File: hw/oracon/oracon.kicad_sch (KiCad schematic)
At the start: 108 parts, among them J2 SIM_Card, J3 USB_A, J4 Conn_Coaxial, J5 USB_C_Receptacle_USB2.0_16P, Q1 SS8050, Q2 SS8050, Q3 SS8050, Q5 SS8050, SW1 SW_Push, U1 TP5100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

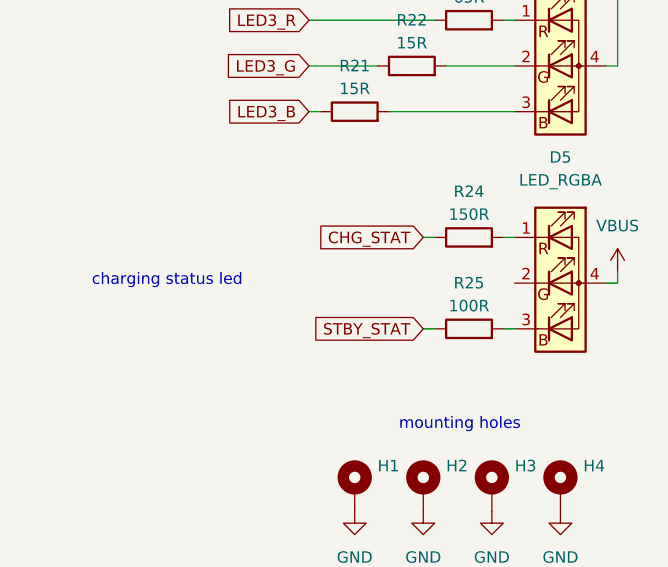
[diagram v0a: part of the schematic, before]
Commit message: Moved charging LED to green channel
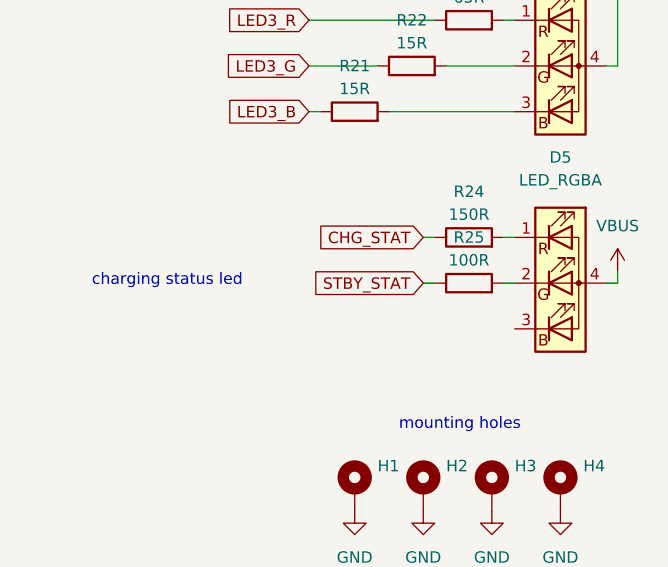
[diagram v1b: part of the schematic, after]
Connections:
- net at D5.2 (GK): now also R25.2
- net at D5.3 (BK): no longer R25.2
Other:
- moved on the sheet: R25
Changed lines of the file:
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@@
 	(wire
 		(pts
-			(xy 384.81 116.84) (xy 386.08 116.84)
-		)
-		(stroke
-			(width 0)
-			(type default)
-		)
-	)
-	(wire
-		(pts
 			(xy 278.13 270.51) (xy 278.13 271.78)
 		)
@@
 	(wire
 		(pts
+			(xy 384.81 111.76) (xy 386.08 111.76)
+		)
+		(stroke
+			(width 0)
+			(type default)
+		)
+	)
+	(wire
+		(pts
 			(xy 60.96 31.75) (xy 62.23 31.75)
 		)
@@
 	(wire
 		(pts
-			(xy 375.92 116.84) (xy 377.19 116.84)
-		)
-		(stroke
-			(width 0)
-			(type default)
-		)
-	)
-	(wire
-		(pts
 			(xy 209.55 36.83) (xy 209.55 19.05)
 		)
@@
 	(wire
 		(pts
+			(xy 375.92 111.76) (xy 377.19 111.76)
+		)
+		(stroke
+			(width 0)
+			(type default)
+		)
+	)
+	(wire
+		(pts
 			(xy 107.95 50.8) (xy 107.95 49.53)
 		)
@@
 		)
 	)
-	(global_label "STBY_STAT"
-		(shape input)
-		(at 375.92 116.84 180)
-		(fields_autoplaced yes)
-		(effects
-			(font
-				(size 1.27 1.27)
-			)
-			(justify right)
-		)
-		(property "Intersheetrefs" "${INTERSHEET_REFS}"
-			(at 363.1982 116.84 0)
-			(effects
-				(font
-					(size 1.27 1.27)
-				)
-				(justify right)
-				(hide yes)
-			)
-		)
-	)
 	(global_label "LED2_B"
 		(shape input)
@@
 		)
 	)
+	(global_label "STBY_STAT"
+		(shape input)
+		(at 375.92 111.76 180)
+		(fields_autoplaced yes)
+		(effects
+			(font
+				(size 1.27 1.27)
+			)
+			(justify right)
+		)
+		(property "Intersheetrefs" "${INTERSHEET_REFS}"
+			(at 363.1982 111.76 0)
+			(effects
+				(font
+					(size 1.27 1.27)
+				)
+				(justify right)
+				(hide yes)
+			)
+		)
+	)
 	(global_label "USB_SI_N"
 		(shape input)
@@
 	(symbol
 		(lib_id "Device:R")
-		(at 381 116.84 90)
+		(at 381 111.76 90)
 		(unit 1)
 		(exclude_from_sim no)
@@
 		(fields_autoplaced yes)
 		(property "Reference" "R25"
-			(at 381 111.76 90)
+			(at 381 106.68 90)
 			(effects
 				(font
@@
 		)
 		(property "Value" "100R"
-			(at 381 114.3 90)
+			(at 381 109.22 90)
 			(effects
 				(font
@@
 		)
 		(property "Footprint" "Resistor_SMD:R_0402_1005Metric"
-			(at 381 118.618 90)
+			(at 381 113.538 90)
 			(effects
 				(font
@@
 		)
 		(property "Datasheet" "~"
-			(at 381 116.84 0)
+			(at 381 111.76 0)
 			(effects
 				(font
@@
 		)
 		(property "Description" "Resistor"
-			(at 381 116.84 0)
+			(at 381 111.76 0)
 			(effects
 				(font
@@
 		)
 		(instances
-			(project "nbiot_esp32s3_hat"
+			(project "oracon"
 				(path "/7501ec1f-5c34-40ce-b7e3-cacc6e1961d1"
 					(reference "R25")

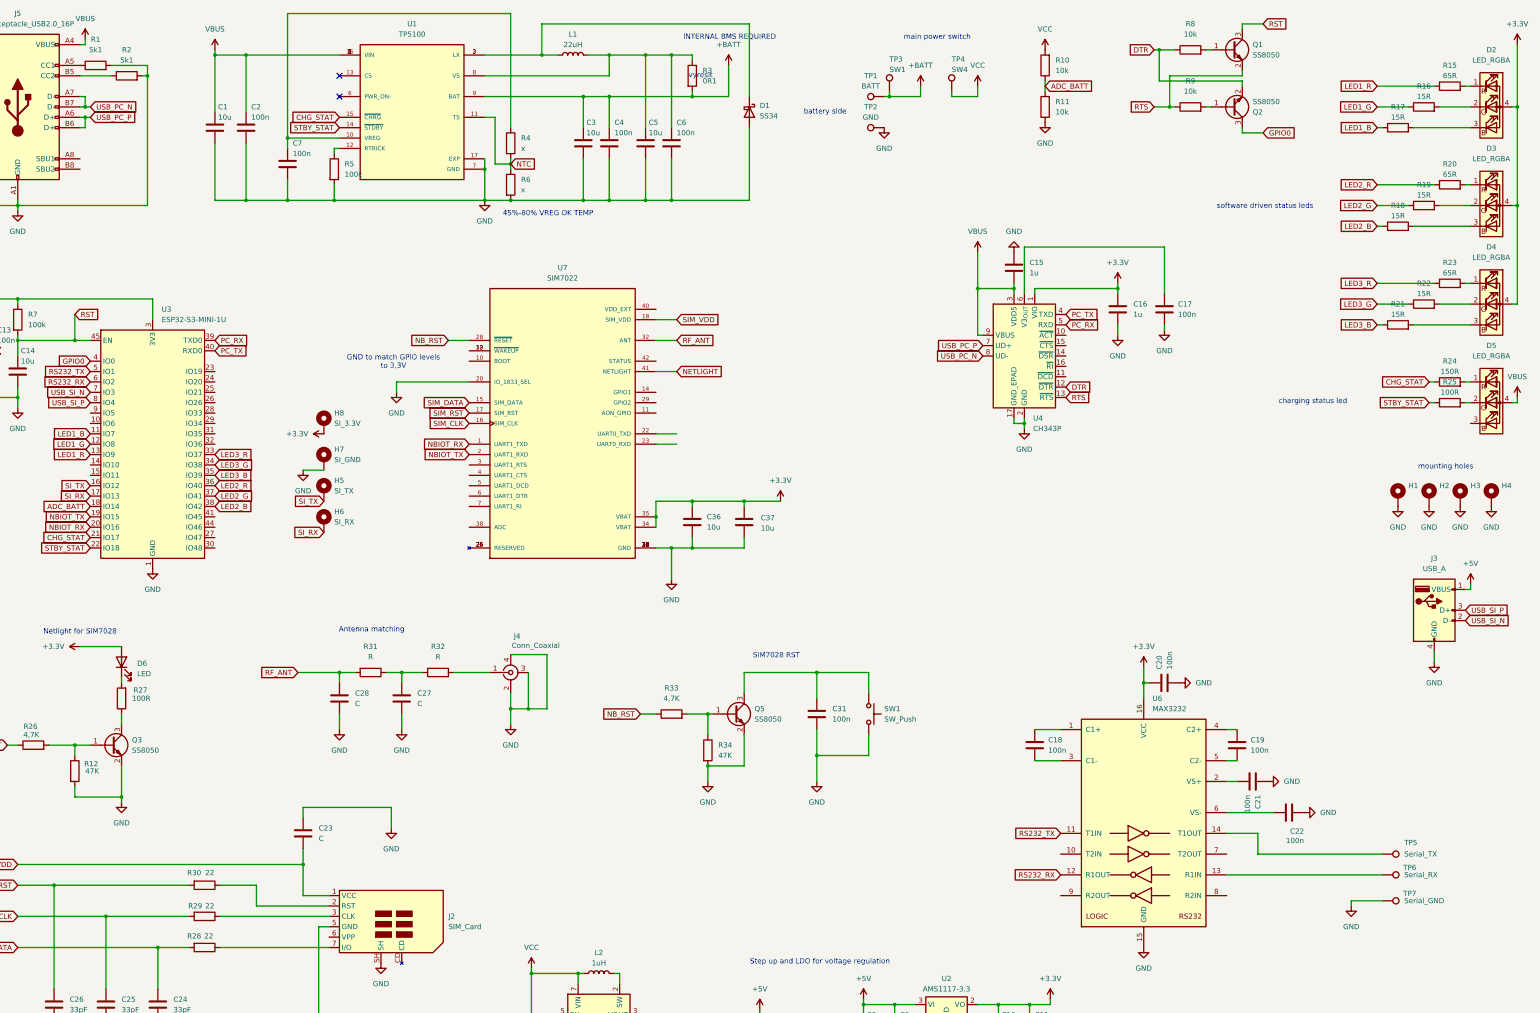
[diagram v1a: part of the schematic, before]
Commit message: Unconnected schema fix
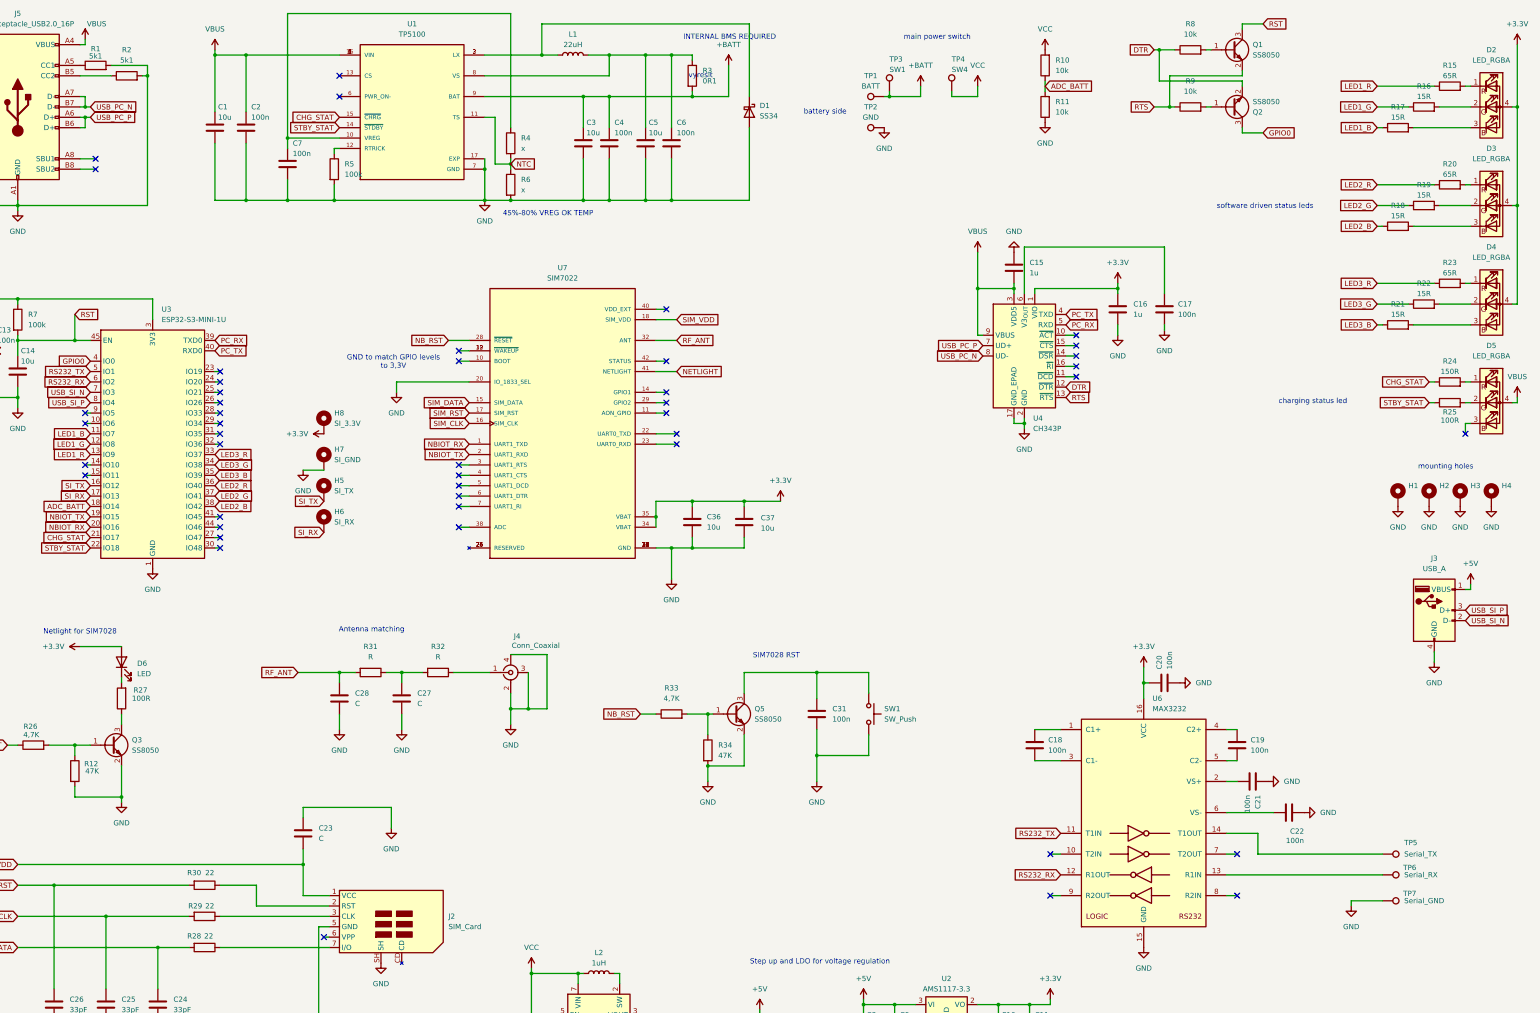
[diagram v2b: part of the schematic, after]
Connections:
- no-connect marks 2 -> 46

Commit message: check
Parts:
- C27, C28: footprint Capacitor_SMD:C_0603_1608Metric -> Capacitor_SMD:C_0402_1005Metric
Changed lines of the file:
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@@
 			)
 		)
-		(property "Footprint" "Capacitor_SMD:C_0603_1608Metric"
+		(property "Footprint" "Capacitor_SMD:C_0402_1005Metric"
 			(at 110.1852 187.96 0)
 			(effects
@@
 			)
 		)
-		(property "Footprint" "Capacitor_SMD:C_0603_1608Metric"
+		(property "Footprint" "Capacitor_SMD:C_0402_1005Metric"
 			(at 125.4252 187.96 0)
 			(effects

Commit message: finishing before ordering
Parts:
- C1, C10, C12, C14, C3, C35, C36, C37, C5, C8: lcsc (none) -> C15850
- C11, C13, C17, C18, C19, C2, C20, C21, C22, C31, C4, C6, C7, C9: lcsc (none) -> C5137468
- C15, C16: lcsc (none) -> C6119852
- C23: value C -> 104; lcsc (none) -> C14663
- C24, C25, C26: lcsc (none) -> C1562
- C27, C28: value C -> DNP
- C32, C33, C34: lcsc (none) -> C5674
- D1: lcsc (none) -> C8678
- D2, D3, D4, D5: lcsc (none) -> C2827321
- D6: lcsc (none) -> C19171390
- J2: value SIM_Card -> SIM_Holder; lcsc (none) -> C2962044
- J3: lcsc (none) -> C3034180
- J4: lcsc (none) -> C41432125
- J5: lcsc (none) -> C5342196
- L1: lcsc (none) -> C5189960
- L2: lcsc (none) -> C5189744
- Q1, Q2, Q3, Q5: lcsc (none) -> C2150
- R1, R2: lcsc (none) -> C25905
- R10, R11, R8, R9: lcsc (none) -> C60490
- R12, R34: lcsc (none) -> C25792
- R13: lcsc (none) -> C5159692
- R14, R5, R7: lcsc (none) -> C60491
- R15, R20, R23: lcsc (none) -> C3016024
- R16, R17, R18, R19, R21, R22: lcsc (none) -> C2909323
- R24: lcsc (none) -> C25082
- R25, R27: lcsc (none) -> C25076
- R26, R33: lcsc (none) -> C25900
- R28, R29, R30: lcsc (none) -> C25092
- R3: value 0R1 -> 120mR; lcsc (none) -> C24435
- R31, R32: value R -> 0R; lcsc (none) -> C106231
- R4, R6: value x -> DNP
- SW3: renamed from SW1; lcsc (none) -> C720477
- TP4: value SW4 -> SW2
- U2: lcsc (none) -> C347222
- U3: lcsc (none) -> C2980299
- U4: lcsc (none) -> C2846043
- U5: lcsc (none) -> C915088
- U6: lcsc (none) -> C19268179
- U7: lcsc (none) -> C7363803
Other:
- note removed: "vyresit"

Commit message: CSQ fix, hw work, cleanup
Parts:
- removed Q5: SS8050, Package_TO_SOT_SMD:SOT-23, symbol Transistor_BJT:SS8050
- removed R33: 4,7K, Resistor_SMD:R_0402_1005Metric, symbol Device:R
- removed R34: 47K, Resistor_SMD:R_0402_1005Metric, symbol Device:R
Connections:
- net GND: now also J3.5 (SHIELD)
- net NB_RST: now also C31.1, SW3.1
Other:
- moved on the sheet: C31, SW3

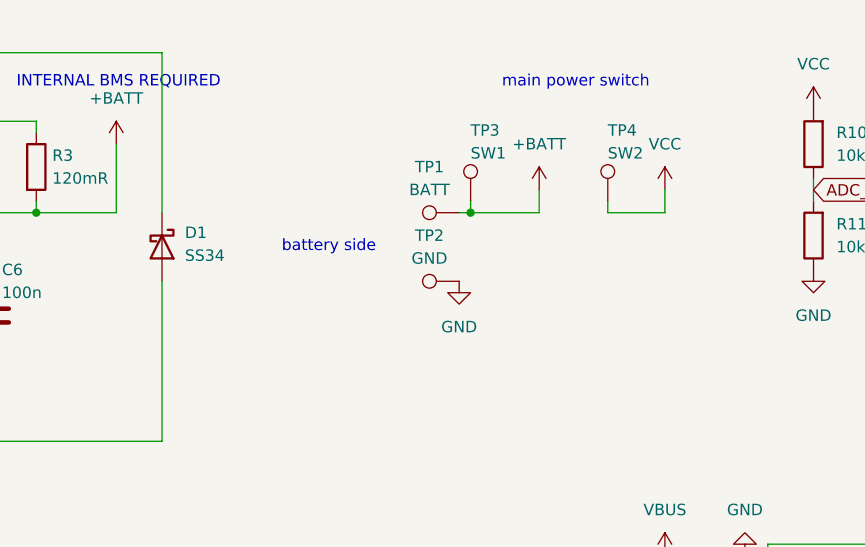
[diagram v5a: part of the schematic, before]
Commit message: made pcb smaller, work to be done
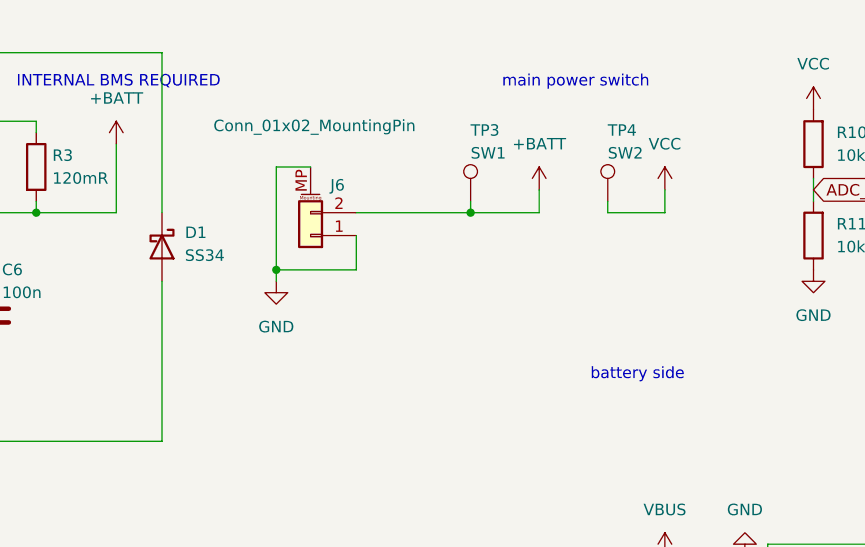
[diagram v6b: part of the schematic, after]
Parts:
- removed TP1: BATT, TestPoint:TestPoint_Pad_D1.5mm, symbol Connector:TestPoint
- removed TP2: GND, TestPoint:TestPoint_Pad_D1.5mm, symbol Connector:TestPoint
- added J6: Conn_01x02_MountingPin, symbol Connector_Generic_MountingPin:Conn_01x02_MountingPin
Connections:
- net +BATT: now also J6.2 (Pin_2)
- net GND: now also J6.1 (Pin_1), J6.MP (MountPin)
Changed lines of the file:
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@@
 	(text "battery side"
 		(exclude_from_sim no)
-		(at 228.092 40.64 0)
+		(at 262.382 54.864 0)
 		(effects
 			(font
@@
 	)
 	(junction
+		(at 222.25 43.18)
+		(diameter 0)
+		(color 0 0 0 0)
+	)
+	(junction
 		(at 189.23 276.86)
 		(diameter 0)
@@
 	(wire
 		(pts
+			(xy 231.14 43.18) (xy 231.14 39.37)
+		)
+		(stroke
+			(width 0)
+			(type default)
+		)
+	)
+	(wire
+		(pts
 			(xy 30.48 245.11) (xy 64.77 245.11)
 		)
@@
 	(wire
 		(pts
-			(xy 243.84 36.83) (xy 242.57 36.83)
-		)
-		(stroke
-			(width 0)
-			(type default)
-		)
-	)
-	(wire
-		(pts
 			(xy 156.21 251.46) (xy 167.64 251.46)
 		)
@@
 	(wire
 		(pts
-			(xy 243.84 35.56) (xy 243.84 36.83)
+			(xy 123.19 109.22) (xy 123.19 106.68)
 		)
 		(stroke
@@
 	(wire
 		(pts
-			(xy 123.19 109.22) (xy 123.19 106.68)
+			(xy 199.39 265.43) (xy 199.39 261.62)
 		)
 		(stroke
@@
 	(wire
 		(pts
-			(xy 199.39 265.43) (xy 199.39 261.62)
+			(xy 39.37 255.27) (xy 39.37 229.87)
 		)
 		(stroke
@@
 	(wire
 		(pts
-			(xy 39.37 255.27) (xy 39.37 229.87)
+			(xy 96.52 62.23) (xy 107.95 62.23)
 		)
 		(stroke
@@
 	(wire
 		(pts
-			(xy 96.52 62.23) (xy 107.95 62.23)
+			(xy 335.28 19.05) (xy 330.2 19.05)
 		)
 		(stroke
@@
 	(wire
 		(pts
-			(xy 335.28 19.05) (xy 330.2 19.05)
+			(xy 222.25 43.18) (xy 222.25 44.45)
 		)
 		(stroke
@@
 	(wire
 		(pts
+			(xy 231.14 36.83) (xy 243.84 36.83)
+		)
+		(stroke
+			(width 0)
+			(type default)
+		)
+	)
+	(wire
+		(pts
 			(xy 237.49 259.08) (xy 245.11 259.08)
 		)
@@
 	(wire
 		(pts
+			(xy 222.25 31.75) (xy 222.25 43.18)
+		)
+		(stroke
+			(width 0)
+			(type default)
+		)
+	)
+	(wire
+		(pts
 			(xy 330.2 33.02) (xy 309.88 33.02)
 		)
@@
 	(wire
 		(pts
+			(xy 222.25 43.18) (xy 231.14 43.18)
+		)
+		(stroke
+			(width 0)
+			(type default)
+		)
+	)
+	(wire
+		(pts
 			(xy 377.19 173.99) (xy 377.19 175.26)
 		)
@@
 	(wire
 		(pts
+			(xy 243.84 36.83) (xy 243.84 35.56)
+		)
+		(stroke
+			(width 0)
+			(type default)
+		)
+	)
+	(wire
+		(pts
 			(xy 175.26 62.23) (xy 184.15 62.23)
 		)
@@
 	(wire
 		(pts
+			(xy 226.06 31.75) (xy 222.25 31.75)
+		)
+		(stroke
+			(width 0)
+			(type default)
+		)
+	)
+	(wire
+		(pts
 			(xy 172.72 276.86) (xy 189.23 276.86)
 		)
@@
 	)
 	(symbol
-		(lib_id "Connector:TestPoint")
-		(at 242.57 36.83 90)
-		(unit 1)
-		(exclude_from_sim no)
-		(in_bom yes)
-		(on_board yes)
-		(dnp no)
-		(fields_autoplaced yes)
-		(property "Reference" "TP1"
-			(at 239.268 31.75 90)
-			(effects
-				(font
-					(size 1.27 1.27)
-				)
-			)
-		)
-		(property "Value" "BATT"
-			(at 239.268 34.29 90)
-			(effects
-				(font
-					(size 1.27 1.27)
-				)
-			)
-		)
-		(property "Footprint" "TestPoint:TestPoint_Pad_D1.5mm"
-			(at 242.57 31.75 0)
-			(effects
-				(font
-					(size 1.27 1.27)
-				)
-				(hide yes)
-			)
-		)
-		(property "Datasheet" "~"
-			(at 242.57 31.75 0)
-			(effects
-				(font
-					(size 1.27 1.27)
-				)
-				(hide yes)
-			)
-		)
-		(property "Description" "test point"
-			(at 242.57 36.83 0)
-			(effects
-				(font
-					(size 1.27 1.27)
-				)
-				(hide yes)
-			)
-		)
-		(pin "1"
-		)
-		(instances
-			(project ""
-				(path "/7501ec1f-5c34-40ce-b7e3-cacc6e1961d1"
-					(reference "TP1")
-					(unit 1)
-				)
-			)
-		)
-	)
-	(symbol
 		(lib_id "Transistor_BJT:SS8050")
 		(at 327.66 39.37 0)
@@
 	)
 	(symbol
+		(lib_id "Connector_Generic_MountingPin:Conn_01x02_MountingPin")
+		(at 226.06 39.37 180)
+		(unit 1)
+		(exclude_from_sim no)
+		(in_bom yes)
+		(on_board yes)
+		(dnp no)
+		(property "Reference" "J6"
+			(at 229.87 33.782 0)
+			(effects
+				(font
+					(size 1.27 1.27)
+				)
+				(justify left)
+			)
+		)
+		(property "Value" "Conn_01x02_MountingPin"
+			(at 237.744 27.178 0)
+			(effects
+				(font
+					(size 1.27 1.27)
+				)
+				(justify left)
+			)
+		)
+		(property "Footprint" ""
+			(at 226.06 39.37 0)
+			(effects
+				(font
+					(size 1.27 1.27)
+				)
+				(hide yes)
+			)
+		)
+		(property "Datasheet" "~"
+			(at 226.06 39.37 0)
+			(effects
+				(font
+					(size 1.27 1.27)
+				)
+				(hide yes)
+			)
+		)
+		(property "Description" "Generic connectable mounting pin connector, single row, 01x02, script generated (kicad-library-utils/schlib/autogen/connector/)"
+			(at 226.06 39.37 0)
+			(effects
+				(font
+					(size 1.27 1.27)
+				)
+				(hide yes)
+			)
+		)
+		(pin "1"
+		)
+		(pin "2"
+		)
+		(pin "MP"
+		)
+		(instances
+			(project ""
+				(path "/7501ec1f-5c34-40ce-b7e3-cacc6e1961d1"
+					(reference "J6")
+					(unit 1)
+				)
+			)
+		)
+	)
+	(symbol
 		(lib_id "power:GND")
 		(at 100.33 128.27 0)
@@
 	(symbol
 		(lib_id "power:GND")
-		(at 242.57 44.45 0)
+		(at 222.25 44.45 0)
 		(unit 1)
 		(exclude_from_sim no)
@@
 		(fields_autoplaced yes)
 		(property "Reference" "#PWR04"
-			(at 242.57 50.8 0)
+			(at 222.25 50.8 0)
 			(effects
 				(font
@@
 		)
 		(property "Value" "GND"
-			(at 242.57 49.53 0)
+			(at 222.25 49.53 0)
 			(effects
 				(font
@@
 		)
 		(property "Footprint" ""
-			(at 242.57 44.45 0)
+			(at 222.25 44.45 0)
 			(effects
 				(font
@@
 		)
 		(property "Datasheet" ""
-			(at 242.57 44.45 0)
+			(at 222.25 44.45 0)
 			(effects
 				(font
@@
 		)
 		(property "Description" "Power symbol creates a global label with name \"GND\" , ground"
-			(at 242.57 44.45 0)
+			(at 222.25 44.45 0)
 			(effects
 				(font
@@
 					(unit 1)
 				)
-			)
-		)
-	)
-	(symbol
-		(lib_id "Connector:TestPoint")
-		(at 242.57 44.45 90)
-		(unit 1)
-		(exclude_from_sim no)
-		(in_bom yes)
-		(on_board yes)
-		(dnp no)
-		(fields_autoplaced yes)
-		(property "Reference" "TP2"
-			(at 239.268 39.37 90)
-			(effects
-				(font
-					(size 1.27 1.27)
-				)
-			)
-		)
-		(property "Value" "GND"
-			(at 239.268 41.91 90)
-			(effects
-				(font
-					(size 1.27 1.27)
-				)
-			)
-		)
-		(property "Footprint" "TestPoint:TestPoint_Pad_D1.5mm"
-			(at 242.57 39.37 0)
-			(effects
-				(font
-					(size 1.27 1.27)
-				)
-				(hide yes)
-			)
-		)
-		(property "Datasheet" "~"
-			(at 242.57 39.37 0)
-			(effects
-				(font
-					(size 1.27 1.27)
-				)
-				(hide yes)
-			)
-		)
-		(property "Description" "test point"
-			(at 242.57 44.45 0)
-			(effects
-				(font
-					(size 1.27 1.27)
-				)
-				(hide yes)
-			)
-		)
-		(pin "1"
-		)
-		(instances
-			(project "nbiot_esp32s3_hat"
-				(path "/7501ec1f-5c34-40ce-b7e3-cacc6e1961d1"
-					(reference "TP2")
-					(unit 1)
-				)
